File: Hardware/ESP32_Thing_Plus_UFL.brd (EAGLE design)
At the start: 22.9 x 58.4 mm, 112 parts, among them Q1 2.5A/30V, Q2 MBT3904DW1T1, U1 MCP73831, U3 AP2112K-3.3V, U4 CP210X, U5 ESP-WROOM-32EU

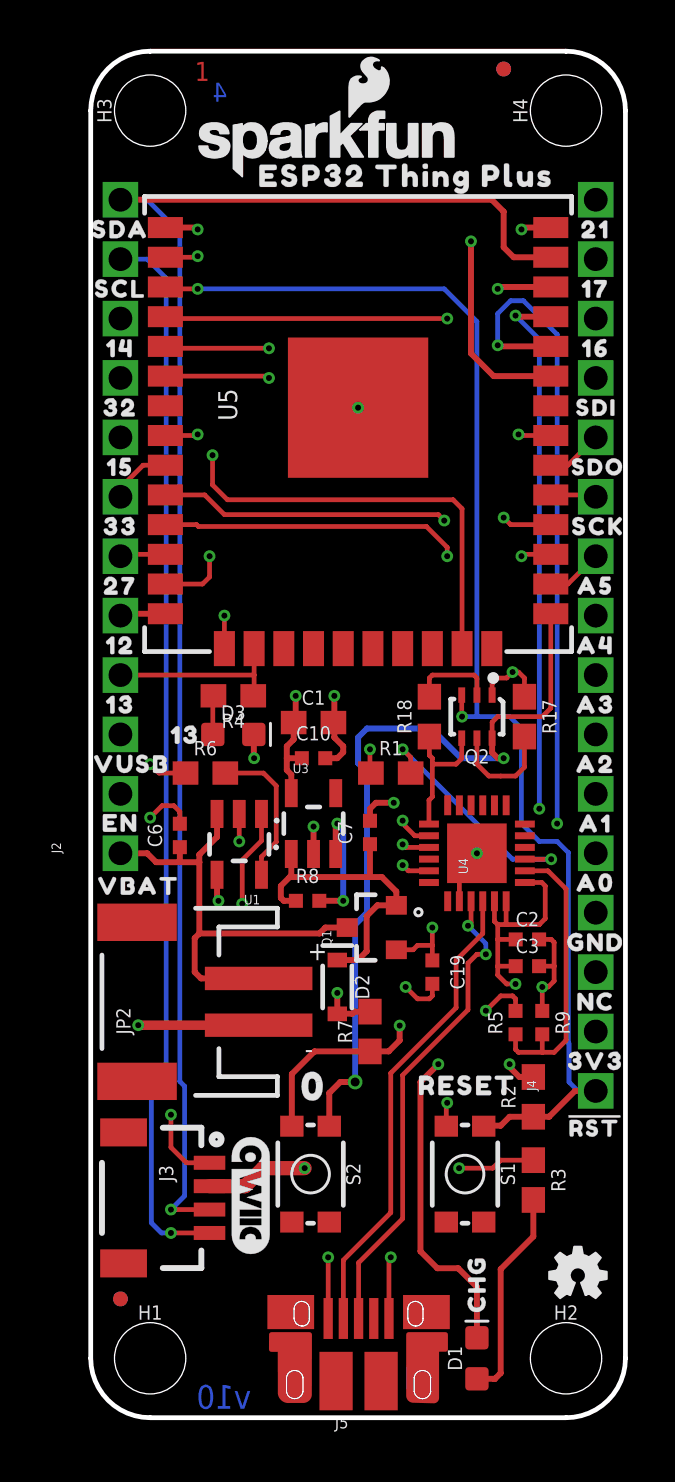
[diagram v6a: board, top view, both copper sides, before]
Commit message: updated ESP32EU footprint to match gnd pad array from datasheet
-also added gnd pours to top and bottom copper
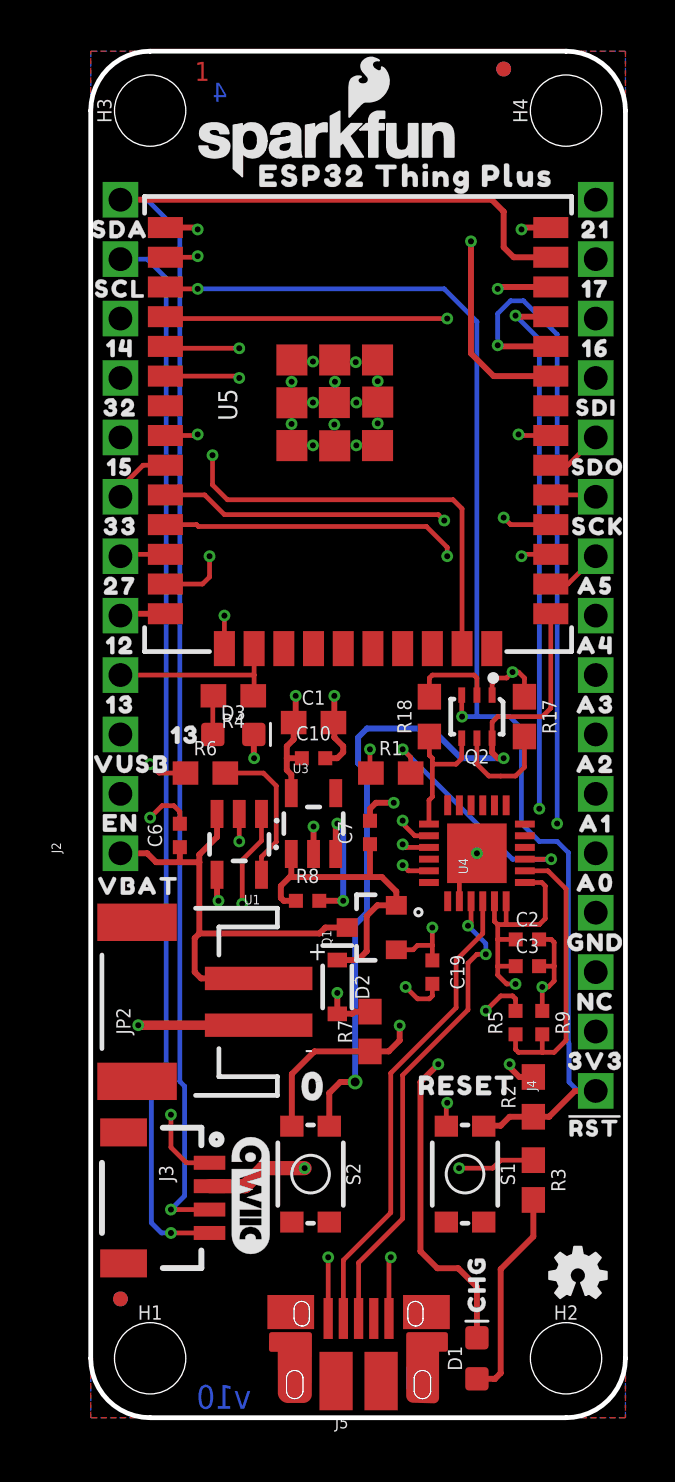
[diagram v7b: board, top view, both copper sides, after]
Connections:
- net GND: now also U5.P$1, U5.P$2, U5.P$3, U5.P$4, U5.P$5, U5.P$6, U5.P$7, U5.P$8
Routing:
- net A2: track 30.4 -> 32.1 mm
- net A3: track 29.0 -> 30.2 mm
- net GND: vias 19 -> 30
- added copper zone on layer 1, net GND
- added copper zone on layer 16, net GND
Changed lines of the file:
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@@
 <contactref element="U5" pad="1"/>
 <contactref element="U5" pad="15"/>
-<via x="11.43" y="43.18" extent="1-16" drill="0.254"/>
+<via x="8.5862" y="44.288" extent="1-16" drill="0.254"/>
 <contactref element="R9" pad="1"/>
 <via x="19.304" y="18.415" extent="1-16" drill="0.254"/>
@@
 <wire x1="12.192" y1="26.289" x2="12.954" y2="26.289" width="0.254" layer="1"/>
 <wire x1="11.938" y1="26.035" x2="12.192" y2="26.289" width="0.254" layer="1"/>
+<contactref element="U5" pad="P$1"/>
+<contactref element="U5" pad="P$2"/>
+<contactref element="U5" pad="P$3"/>
+<contactref element="U5" pad="P$4"/>
+<contactref element="U5" pad="P$5"/>
+<contactref element="U5" pad="P$6"/>
+<contactref element="U5" pad="P$7"/>
+<contactref element="U5" pad="P$8"/>
+<via x="11.3548" y="43.399" extent="1-16" drill="0.254"/>
+<via x="11.3548" y="41.5702" extent="1-16" drill="0.254"/>
+<via x="9.5006" y="41.5702" extent="1-16" drill="0.254"/>
+<via x="8.5862" y="42.4846" extent="1-16" drill="0.254"/>
+<via x="10.415" y="42.4592" extent="1-16" drill="0.254"/>
+<via x="12.2692" y="42.51" extent="1-16" drill="0.254"/>
+<via x="11.3294" y="45.1262" extent="1-16" drill="0.254"/>
+<via x="9.5006" y="45.1516" extent="1-16" drill="0.254"/>
+<via x="9.5006" y="43.399" extent="1-16" drill="0.254"/>
+<via x="10.4404" y="44.288" extent="1-16" drill="0.254"/>
+<via x="12.2692" y="44.3134" extent="1-16" drill="0.254"/>
+<polygon width="0.2032" layer="1">
+<vertex x="0" y="0"/>
+<vertex x="0" y="58.42"/>
+<vertex x="22.86" y="58.42"/>
+<vertex x="22.86" y="0"/>
+</polygon>
+<polygon width="0.2032" layer="16">
+<vertex x="0" y="0"/>
+<vertex x="22.86" y="0"/>
+<vertex x="22.86" y="58.42"/>
+<vertex x="0" y="58.42"/>
+</polygon>
 </signal>
 <signal name="DTR">
@@
 <signal name="A2">
 <contactref element="J4" pad="7"/>
-<wire x1="3.192" y1="44.53" x2="7.54" y2="44.53" width="0.2032" layer="1"/>
-<wire x1="7.54" y1="44.53" x2="7.62" y2="44.45" width="0.2032" layer="1"/>
-<via x="7.62" y="44.45" extent="1-16" drill="0.254"/>
-<wire x1="7.62" y1="44.45" x2="16.002" y2="44.45" width="0.2032" layer="15"/>
-<wire x1="16.002" y1="44.45" x2="16.8148" y2="43.6372" width="0.2032" layer="15"/>
+<wire x1="3.192" y1="44.53" x2="6.27" y2="44.53" width="0.2032" layer="1"/>
+<wire x1="6.27" y1="44.53" x2="6.35" y2="44.45" width="0.2032" layer="1"/>
+<via x="6.35" y="44.45" extent="1-16" drill="0.254"/>
+<wire x1="13.97" y1="46.482" x2="8.382" y2="46.482" width="0.2032" layer="15"/>
+<wire x1="6.35" y1="44.45" x2="8.382" y2="46.482" width="0.2032" layer="15"/>
+<wire x1="13.97" y1="46.482" x2="16.8148" y2="43.6372" width="0.2032" layer="15"/>
 <wire x1="16.8148" y1="43.6372" x2="16.8148" y2="34.026225" width="0.2032" layer="15"/>
 <wire x1="21.59" y1="29.251025" x2="21.59" y2="29.21" width="0.2032" layer="15"/>
@@
 <contactref element="J4" pad="8"/>
 <wire x1="3.192" y1="45.8" x2="3.272" y2="45.72" width="0.2032" layer="1"/>
-<wire x1="3.272" y1="45.72" x2="7.62" y2="45.72" width="0.2032" layer="1"/>
-<via x="7.62" y="45.72" extent="1-16" drill="0.254"/>
-<wire x1="15.706975" y1="45.72" x2="19.05" y2="42.376975" width="0.2032" layer="15"/>
-<wire x1="19.05" y1="42.376975" x2="19.05" y2="34.29" width="0.2032" layer="15"/>
-<wire x1="7.62" y1="45.72" x2="15.706975" y2="45.72" width="0.2032" layer="15"/>
+<wire x1="3.272" y1="45.72" x2="6.35" y2="45.72" width="0.2032" layer="1"/>
+<via x="6.35" y="45.72" extent="1-16" drill="0.254"/>
+<wire x1="14.030575" y1="47.2694" x2="19.05" y2="42.249975" width="0.2032" layer="15"/>
+<wire x1="19.05" y1="42.249975" x2="19.05" y2="34.29" width="0.2032" layer="15"/>
+<wire x1="6.35" y1="45.72" x2="7.8994" y2="47.2694" width="0.2032" layer="15"/>
+<wire x1="14.030575" y1="47.2694" x2="7.8994" y2="47.2694" width="0.2032" layer="15"/>
 <wire x1="19.05" y1="34.29" x2="21.59" y2="31.75" width="0.2032" layer="15"/>
 <contactref element="U5" pad="5"/>
